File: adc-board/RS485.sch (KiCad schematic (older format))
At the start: 5 parts, among them J6 54601-908WPLF, U14 ISL83490

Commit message: adc board schematic tweaks and complete relayout
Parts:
- C60: renamed from C28; footprint Capacitors_SMD:C_0805_HandSoldering -> Capacitors_SMD:C_0805
- R60: renamed from R30; footprint Resistors_SMD:R_0805_HandSoldering -> Resistors_SMD:R_0805
- R61: renamed from R24; footprint Resistors_SMD:R_0805_HandSoldering -> Resistors_SMD:R_0805
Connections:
- net labels added: +5V
- net labels removed: +12V
- wire segments 38 -> 40
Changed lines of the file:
@@
 $Descr A4 11693 8268
 encoding utf-8
-Sheet 2 2
+Sheet 2 3
 Title ""
 Date ""
@@
 	1    0    0    -1
 $EndComp
-$Comp
-L power:+12V #PWR?
-U 1 1 630647BE
-P 6800 3250
-AR Path="/630647BE" Ref="#PWR?"  Part="1"
-AR Path="/62FDE2B6/630647BE" Ref="#PWR0135"  Part="1"
-F 0 "#PWR0135" H 6800 3100 50  0001 C CNN
-F 1 "+12V" H 6815 3423 50  0000 C CNN
-F 2 "" H 6800 3250 50  0001 C CNN
-F 3 "" H 6800 3250 50  0001 C CNN
-	1    6800 3250
-	1    0    0    -1
-$EndComp
 Wire Wire Line
 	6700 4000 7100 4000
@@
 	6900 3600 6900 3800
 Wire Wire Line
-	7100 3800 6900 3800
+	7100 3800 7000 3800
 Connection ~ 6900 3800
 Wire Wire Line
@@
 	6800 3250 6800 3700
 Wire Wire Line
-	7100 3700 6800 3700
+	7100 3700 7000 3700
 Connection ~ 6800 3700
 Wire Wire Line
@@
 	6550 3600 6300 3600
 $Comp
-L Device:R_Small_US R24
+L Device:R_Small_US R61
 U 1 1 6316A97F
 P 6400 3500
-F 0 "R24" V 6195 3500 50  0000 C CNN
+F 0 "R61" V 6195 3500 50  0000 C CNN
 F 1 "120" V 6286 3500 50  0000 C CNN
-F 2 "Resistors_SMD:R_0805_HandSoldering" H 6400 3500 50  0001 C CNN
+F 2 "Resistors_SMD:R_0805" H 6400 3500 50  0001 C CNN
 F 3 "~" H 6400 3500 50  0001 C CNN
 	1    6400 3500
@@
 	6500 3700 6250 3700
 $Comp
-L Device:C_Small C28
+L Device:C_Small C60
 U 1 1 6316C6B4
 P 3600 3750
-F 0 "C28" H 3692 3796 50  0000 L CNN
+F 0 "C60" H 3692 3796 50  0000 L CNN
 F 1 "DC" H 3692 3705 50  0000 L CNN
-F 2 "Capacitors_SMD:C_0805_HandSoldering" H 3600 3750 50  0001 C CNN
+F 2 "Capacitors_SMD:C_0805" H 3600 3750 50  0001 C CNN
 F 3 "~" H 3600 3750 50  0001 C CNN
 	1    3600 3750
@@
 Note that ethernet cables don't flip pins.\nMain board MUST connect different pins to the receptable.
 $Comp
-L Device:R_Small_US R30
+L Device:R_Small_US R60
 U 1 1 640640AD
 P 6400 4050
-F 0 "R30" V 6195 4050 50  0000 C CNN
+F 0 "R60" V 6195 4050 50  0000 C CNN
 F 1 "120" V 6286 4050 50  0000 C CNN
-F 2 "Resistors_SMD:R_0805_HandSoldering" H 6400 4050 50  0001 C CNN
+F 2 "Resistors_SMD:R_0805" H 6400 4050 50  0001 C CNN
 F 3 "~" H 6400 4050 50  0001 C CNN
 	1    6400 4050
@@
 Wire Wire Line
 	6500 3900 6250 3900
+$Comp
+L power:+5V #PWR0133
+U 1 1 60B07DD5
+P 6800 3250
+F 0 "#PWR0133" H 6800 3100 50  0001 C CNN
+F 1 "+5V" H 6815 3423 50  0000 C CNN
+F 2 "" H 6800 3250 50  0001 C CNN
+F 3 "" H 6800 3250 50  0001 C CNN
+	1    6800 3250
+	1    0    0    -1
+$EndComp
+$Comp
+L power:PWR_FLAG #FLG0101
+U 1 1 60B45280
+P 7000 3700
+F 0 "#FLG0101" H 7000 3775 50  0001 C CNN
+F 1 "PWR_FLAG" H 7000 3873 50  0000 C CNN
+F 2 "" H 7000 3700 50  0001 C CNN
+F 3 "~" H 7000 3700 50  0001 C CNN
+	1    7000 3700
+	1    0    0    -1
+$EndComp
+Connection ~ 7000 3700
+Wire Wire Line
+	7000 3700 6800 3700
+$Comp
+L power:PWR_FLAG #FLG0102
+U 1 1 60B4653B
+P 7000 3800
+F 0 "#FLG0102" H 7000 3875 50  0001 C CNN
+F 1 "PWR_FLAG" H 7000 3973 50  0000 C CNN
+F 2 "" H 7000 3800 50  0001 C CNN
+F 3 "~" H 7000 3800 50  0001 C CNN
+	1    7000 3800
+	1    0    0    -1
+$EndComp
+Connection ~ 7000 3800
+Wire Wire Line
+	7000 3800 6900 3800
 $EndSCHEMATC

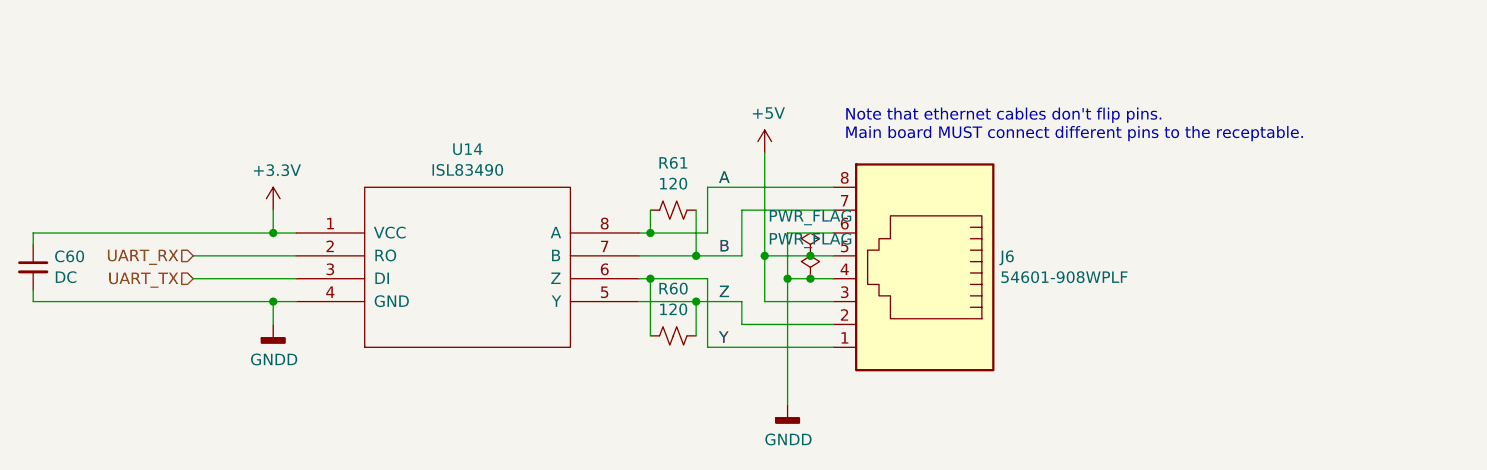
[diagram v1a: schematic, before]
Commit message: correct RS485 termination resistors, adjust ground pours
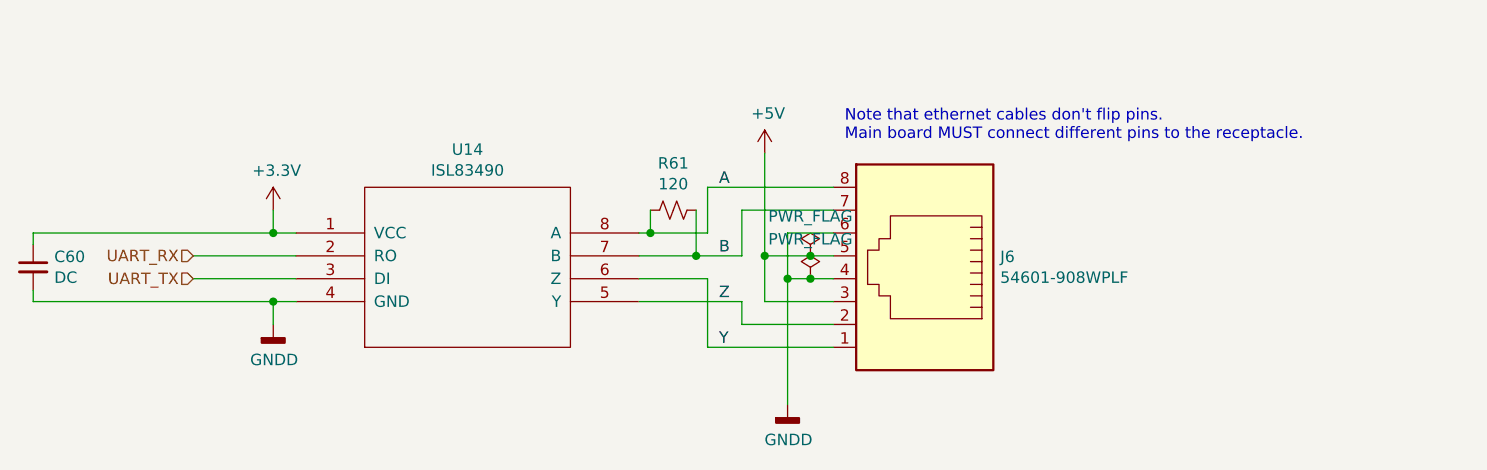
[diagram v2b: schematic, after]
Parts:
- removed R60: 120, Resistors_SMD:R_0805, symbol Device:R_Small_US
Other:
- note added: "Note that ethernet cables don't flip pins.\nMain board MUST connect different pins to the receptacle."
- note removed: "Note that ethernet cables don't flip pins.\nMain board MUST connect different pins to the receptable."
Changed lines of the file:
@@
 Connection ~ 4650 3900
-Wire Wire Line
-	6550 3800 6300 3800
 Wire Wire Line
 	6550 3800 6550 4100
 Wire Wire Line
 	6700 4000 6700 3900
-Wire Wire Line
-	6700 3900 6500 3900
 Text Label 6600 3400 0    50   ~ 0
 A
@@
 Y
 Text Notes 7150 3200 0    50   ~ 0
-Note that ethernet cables don't flip pins.\nMain board MUST connect different pins to the receptable.
-$Comp
-L Device:R_Small_US R60
-U 1 1 640640AD
-P 6400 4050
-F 0 "R60" V 6195 4050 50  0000 C CNN
-F 1 "120" V 6286 4050 50  0000 C CNN
-F 2 "Resistors_SMD:R_0805" H 6400 4050 50  0001 C CNN
-F 3 "~" H 6400 4050 50  0001 C CNN
-	1    6400 4050
-	0    1    1    0
-$EndComp
-Wire Wire Line
-	6300 4050 6300 3800
-Connection ~ 6300 3800
-Wire Wire Line
-	6300 3800 6250 3800
-Wire Wire Line
-	6500 4050 6500 3900
-Connection ~ 6500 3900
-Wire Wire Line
-	6500 3900 6250 3900
+Note that ethernet cables don't flip pins.\nMain board MUST connect different pins to the receptacle.
 $Comp
 L power:+5V #PWR0133
@@
 Wire Wire Line
 	7000 3800 6900 3800
+Wire Wire Line
+	6250 3800 6550 3800
+Wire Wire Line
+	6250 3900 6700 3900
 $EndSCHEMATC

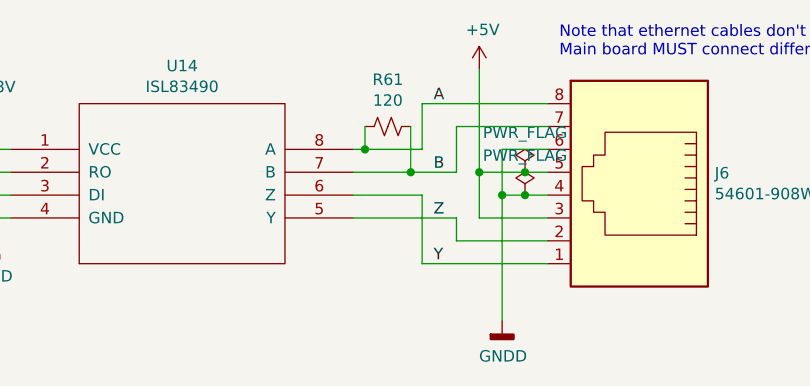
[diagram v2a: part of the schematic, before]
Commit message: Fix swapped RS485 Z/Y pins. Add reset supervisor and 4 pin USB header.
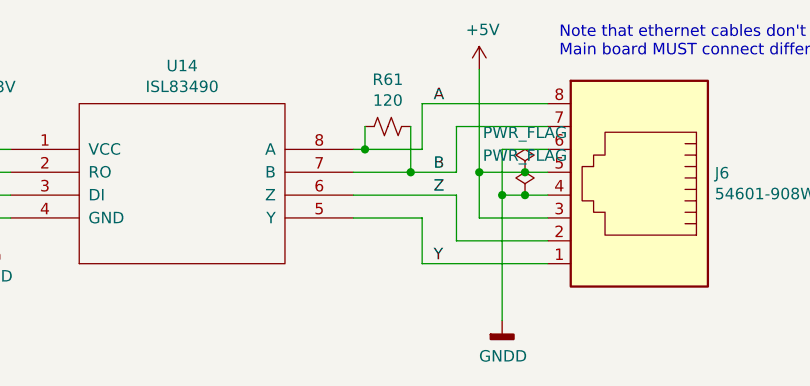
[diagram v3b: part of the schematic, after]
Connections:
- net Y: now also U14.5 (Y); no longer U14.6 (Z)
- net Z: now also U14.6 (Z); no longer U14.5 (Y)
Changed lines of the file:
@@
 Connection ~ 4650 3900
 Wire Wire Line
-	6550 3800 6550 4100
-Wire Wire Line
-	6700 4000 6700 3900
+	6700 4000 6700 3800
 Text Label 6600 3400 0    50   ~ 0
 A
 Text Label 6600 3700 0    50   ~ 0
 B
-Text Label 6600 3900 0    50   ~ 0
+Text Label 6600 3800 0    50   ~ 0
 Z
 Text Label 6600 4100 0    50   ~ 0
@@
 	7000 3800 6900 3800
 Wire Wire Line
-	6250 3800 6550 3800
+	6250 3800 6700 3800
 Wire Wire Line
-	6250 3900 6700 3900
+	6550 4100 6550 3900
+Wire Wire Line
+	6550 3900 6250 3900
 $EndSCHEMATC
